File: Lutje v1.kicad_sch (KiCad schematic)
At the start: 9 parts, among them J1 U.FL-R-SMT_10_, U1 ESP32-S3FH4R2, U2 SX1281IMLTRT, U3 AMS1117-3.3, U4 DRV8212DRLR, U5 DRV8212DRLR, U6 DRV8212DRLR

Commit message: initial schematic work
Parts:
- removed FL1: 2450FM07D0034T, footprints:FIL_2450FM07D0034T, symbol 2450FM07D0034T:2450FM07D0034T
- removed J1: U.FL-R-SMT_10_, footprints:HIROSE_U.FL-R-SMT_10_, symbol U.FL-R-SMT_10_:U.FL-R-SMT_10_
- removed U1: ESP32-S3FH4R2, footprints:QFN40P700X700X90-57N, symbol ESP32-S3FH4R2:ESP32-S3FH4R2
- removed U2: SX1281IMLTRT, footprints:XCVR_SX1281IMLTRT, symbol SX1281IMLTRT:SX1281IMLTRT
- removed U3: AMS1117-3.3, footprints:SOT229P700X180-4N, symbol AMS1117-3.3:AMS1117-3.3
- removed U4, U5, U6: DRV8212DRLR, footprints:drv8212drlr, symbol drv8212drlr:DRV8212DRLR
- removed XTAL1: NX2016SA-52MHZ-EXS00A-CS07103, footprints:OSCCC200X160X50N, symbol NX2016SA-52MHZ-EXS00A-CS07103:NX2016SA-52MHZ-EXS00A-CS07103
- added C1, C4: 10n, symbol Device:C
- added C10, C11, C6, C7, C8, C9: C, symbol Device:C
- added C2, C3: 100n, symbol Device:C
- added C5: 470n, symbol Device:C
- added J1, J3, J4, J5: Conn_01x02, symbol Connector_Generic:Conn_01x02
- added J2: Conn_Coaxial, Connector_Coaxial:U.FL_Hirose_U.FL-R-SMT-1_Vertical, symbol Connector:Conn_Coaxial
- added U1: SX1280, Package_DFN_QFN:QFN-24-1EP_4x4mm_P0.5mm_EP2.7x2.7mm, symbol .local:SX1280
- added U11, U12, U7: DRV8212DRL, Package_TO_SOT_SMD:SOT-563, symbol .local:DRV8212DRL
- added U2: 2450FM07D0034, symbol .local:2450FM07D0034
- added U3: ESP32-S3S3FN8, Package_DFN_QFN:QFN-56-1EP_7x7mm_P0.4mm_EP5.6x5.6mm, symbol PCM_Espressif:ESP32-S3
- added U8: AMS1117-3.3, Package_TO_SOT_SMD:SOT-223-3_TabPin2, symbol Regulator_Linear:AMS1117-3.3
- added Y1: XC21M4-52.000-F10NNHPL, symbol Device:Crystal_GND24
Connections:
- net GND: now also C1.2, C10.2, C11.2, C2.2, C3.2, C4.2, C5.2, C6.2, C7.2, C8.2, C9.2, J5.1 (Pin_1), U1.13 (GND), U1.20 (GND), U1.21 (GND), U1.23 (GND), U1.24 (GND), U1.25 (GND), U1.5 (GND), U11.3 (GND), U12.3 (GND), U2.2 (GND), U2.4 (GND), U7.3 (GND), U8.1 (GND), Y1.2 (G), Y1.4 (G)
- net VDD3P3: now also U3.2 (VDD3P3), U3.3 (VDD3P3)
- new net: U3.55 (VDDA), U3.56 (VDDA)
- new net +3V3: C2.1, C3.1, C7.1, U1.11 (VBAT_IO), U1.15 (VBAT), U8.2 (VO)
- new net VDC: C10.1, C11.1, C6.1, C8.1, C9.1, J5.2 (Pin_2), U11.5 (VM), U12.5 (VM), U7.5 (VM), U8.3 (VI)
- new net m0_in1: U7.1 (IN1)
- new net m0_in2: U7.2 (IN2)
- new net m0_out1: J1.1 (Pin_1), U7.6 (OUT1)
- new net m0_out2: J1.2 (Pin_2), U7.4 (OUT2)
- new net m1_in1: U11.1 (IN1)
- new net m1_in2: U11.2 (IN2)
- new net m1_out1: J3.1 (Pin_1), U11.6 (OUT1)
- new net m1_out2: J3.2 (Pin_2), U11.4 (OUT2)
- new net m2_in1: U12.1 (IN1)
- new net m2_in2: U12.2 (IN2)
- new net m2_out1: J4.1 (Pin_1), U12.6 (OUT1)
- new net m2_out2: J4.2 (Pin_2), U12.4 (OUT2)
- new net rfio: U1.22 (RFIO), U2.1 (IN)
- new net sx1280_dcc_fb/vdd_in: C4.1, C5.1, U1.12 (DCC_FB), U1.2 (VDD_IN)
- new net sx1280_xta: U1.4 (XTA), Y1.1
- new net sx1280_xtb: U1.6 (XTB), Y1.3
- new net vr_pa: C1.1, U1.1 (VR_PA)
- no-connect marks 0 -> 1
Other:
- note added: "als we maar 2 brushed kanalen willen kunenn we een c3 gebruiken"
- note added: "datasheet beveeld 22uF tantalum aan bij de output. tantalum is irritant en heeft een varierende prijs het is het overwegen waardt om die te vervangen met een keramische mogelijk met een series resisotr om de hogere ESR te simuleren als dat nodig is voor stability. ook DC-bias effecten controleren maar ik vermoed dat dat niet een heel erg groot probleem is bij 3.3V"
- note added: "er moet hier een rf-switch tussen zodat er ook een pcb antenne bij kan"
- note added: "is een bulk capacitor nodig? en hoe groot moet hij dan zijn?"
- note added: "overweeg reverse polarity protection. en maybe een zekering"

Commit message: begin esp inrichting gemaakt
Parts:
- removed J4: Conn_01x02, symbol Connector_Generic:Conn_01x02
- removed U12: DRV8212DRL, Package_TO_SOT_SMD:SOT-563, symbol .local:DRV8212DRL
- added AE1: Antenna, symbol Device:Antenna
- added C12, C17: 1uF, symbol Device:C
- added C13: 10uF, symbol Device:C
- added C14, C15, C18, C25: 100n, symbol Device:C
- added C16: 10n, symbol Device:C
- added C19, C20: TBD, symbol Device:C
- added C21, C22, C23, C24: C, symbol Device:C
- added D1: PWR, symbol Device:LED
- added D2: LED, symbol Device:LED
- added L1: 2.0 nH 500 mA, symbol Device:L
- added L2: TBD, symbol Device:L
- added L3, L4: L, symbol Device:L
- added Q1: AON7403, AON7403:TRANS_AON7403, symbol AON7403:AON7403
- added R1: 10R, symbol Device:R
- added R2: 33R, symbol Device:R
- added R3: 33K, symbol Device:R
- added R4, R5, R6: 10K, symbol Device:R
- added R7, R8: 1K, symbol Device:R
- added SW1: SW_Push, symbol Switch:SW_Push
- added Y2: XXDBBCNANF-40.000000MHZ, symbol Device:Crystal_GND24
- C10, C11: value C -> 100n
- C6: value C -> 10uF
- C7: value C -> 22uF
- J2: footprint Connector_Coaxial:U.FL_Hirose_U.FL-R-SMT-1_Vertical -> (none)
- Y1: lcsc C3034316 -> (none)
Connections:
- net +3V3: now also C11.1, U3.20 (VDD3P3_RTC), U3.46 (VDD3P3_CPU), U3.55 (VDDA), U3.56 (VDDA), C12.1, C13.1, C14.2, C15.2, C16.2, C17.2, D1.2 (A), D2.2 (A), L1.1, R5.2, R6.1
- net GND: now also C12.2, C13.2, C14.1, C15.1, C16.1, C17.1, C18.1, C19.2, C20.2, C21.2, C22.2, C23.2, C24.2, C25.2, R1.2, R4.2, R7.1, SW1.2, Y2.2 (G), Y2.4 (G)
- net VDC: now also Q1.1, Q1.2, Q1.3, R3.1; no longer C10.1, C11.1, J5.2 (Pin_2)
- net VDD3P3: now also C10.1, L1.2
- net at U3.1 (LNA_IN/RF): now also C24.1, L4.2
- net SX1280_RESET: now reaches U3.13 (GPIO8/ADC1_CH7)
- net SX1280_RESET: now also U1.3 (~{RESET})
- net SX1280_DIO1: now reaches U3.14 (GPIO9/ADC1_CH8)
- net SX1280_DIO1: now also U1.8 (DIO1)
- net SS_CTS: now reaches U3.15 (GPIO10/ADC1_CH9)
- net SS_CTS: now also U1.19 (~{SS_CTS})
- net SX1280_MOSI: now reaches U3.16 (GPIO11/ADC2_CH0)
- net SX1280_MOSI: now also U1.17 (MOSI_RX)
- net at U3.17 (GPIO12/ADC2_CH1): now also R2.1
- net SX1280_MISO: now reaches U3.18 (GPIO13/ADC2_CH2)
- net SX1280_MISO: now also U1.16 (MISO_TX)
- net SX1280_BUSY: now reaches U3.19 (GPIO14/ADC2_CH3)
- net SX1280_BUSY: now also U1.7 (BUSY)
- net at U3.29 (VDD_SPI): now also C18.2
- net at U3.4 (CHIP_PU/RESET): now also C25.1, R5.1
- net BOOT: now reaches U3.5 (GPIO0/BOOT)
- net BOOT: now also R6.2, SW1.1
- net at U3.53 (XTAL_N): now also C19.1, Y2.3
- net at U3.54 (XTAL_P): now also L2.2
- net VSENS: now reaches U3.6 (GPIO1/ADC1_CH0)
- net VSENS: now also R3.2, R4.1
- net at U3.7 (GPIO2/ADC1_CH1): now also R8.2
- net SCK: now reaches U1.18 (SCK_~{RTS})
- net SCK: now also R2.2
- net rfio renamed SX1280_RFIO
- net sx1280_dcc_fb/vdd_in renamed SX1280_DCC_FB/VDD_IN
- net sx1280_xta renamed SX1280_XTA
- net sx1280_xtb renamed SX1280_XTB
- net vr_pa renamed SX1280_VR_PA
- new net: C22.1, C23.1, L3.2, L4.1
- new net: C20.1, L2.1, Y2.1
- new net: AE1.1 (A), C21.1, L3.1
- new net: D1.1 (K), R7.2
- new net: Q1.4, R1.1
- new net: J5.2 (Pin_2), Q1.5_8
- new net: D2.1 (K), R8.1
- no-connect marks 1 -> 3
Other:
- note removed: "als we maar 2 brushed kanalen willen kunenn we een c3 gebruiken"
- note removed: "is een bulk capacitor nodig? en hoe groot moet hij dan zijn?"
- note removed: "overweeg reverse polarity protection. en maybe een zekering"
- moved on the sheet: C1, C2, C3, C4, C5, C8, C9, J1, J2, J3, U1, U11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

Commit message: begin esp inrichting gemaakt
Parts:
- U3: value ESP32-S3S3FN8 -> ESP32-S3FN8
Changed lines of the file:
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@@
 			)
 		)
-		(property "Value" "ESP32-S3S3FN8"
+		(property "Value" "ESP32-S3FN8"
 			(at 239.6333 198.12 0)
 			(show_name no)

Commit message: aanpassing aan schematic
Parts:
- removed R2: 33R, symbol Device:R
- removed R6: 10K, symbol Device:R
- Y2: value XXDBBCNANF-40.000000MHZ -> Q22FA12800332; footprint (none) -> Crystal:Crystal_SMD_2016-4Pin_2.0x1.6mm; lcsc (none) -> C255899
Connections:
- net GND: now also U3.57 (GND); no longer C10.2, C11.2, C12.2, C13.2, C18.1
- net SCK: now also U3.17 (GPIO12/ADC2_CH1)
- net lna_matching: now reaches C22.1, C23.1, L3.2, L4.1
- net esp32_xtal_p: now reaches C20.1, L2.1, Y2.1
- net esp32_xtal_n: now reaches C19.1, U3.53 (XTAL_N), Y2.3
- net lna_ant: now reaches AE1.1 (A), C21.1, L3.1
- net chip_pu: now reaches C25.1, R5.1, U3.4 (CHIP_PU/RESET)
- net status_LED_n0: now reaches D2.1 (K), R8.1
- net vdd_spi: now reaches C18.2, U3.29 (VDD_SPI)
- net lna_in: now reaches C24.1, L4.2, U3.1 (LNA_IN/RF)
- net esp32_xtal_p_filtered: now reaches L2.2, U3.54 (XTAL_P)
- net STATUS_LED: now reaches R8.2, U3.7 (GPIO2/ADC1_CH1)
- new net: C10.2, C11.2, C12.2, C13.2, C18.1
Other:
- moved on the sheet: C19, C20, D2, L2, R3, R4, R8, SW1, Y2

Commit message: changed to esp32, added zener/tvs and servo channels
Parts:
- removed AE1: Antenna, symbol Device:Antenna
- removed C24: C, symbol Device:C
- removed C25: 100n, symbol Device:C
- removed L2: TBD, symbol Device:L
- removed L3, L4: L, symbol Device:L
- removed U3: ESP32-S3FN8, Package_DFN_QFN:QFN-56-1EP_7x7mm_P0.4mm_EP5.6x5.6mm, symbol PCM_Espressif:ESP32-S3
- added AE1: Antenna_Chip, symbol Device:Antenna_Chip
- added D3, D4: D_Zener, symbol Device:D_Zener
- added D5: D_TVS, symbol Device:D_TVS
- added J4: Conn_01x02, symbol Connector_Generic:Conn_01x02
- added J6, J8: Conn_01x03, symbol Connector_Generic:Conn_01x03
- added R2: R, symbol Device:R
- added R6: 1k, symbol Device:R
- added U3: ESP32-U4WDH, .local:esp32_2layer_thermalvias, symbol PCM_Espressif:ESP32
- C10, C11, C14, C15: value 100n -> TBD; footprint (none) -> Capacitor_SMD:C_0402_1005Metric
- C12, C17: value 1uF -> 10u; footprint (none) -> Capacitor_SMD:C_0402_1005Metric
- C13: value 10uF -> 10u; footprint (none) -> Capacitor_SMD:C_0402_1005Metric
- C16: value 10n -> 10u; footprint (none) -> Capacitor_SMD:C_0402_1005Metric
- C18: value 100n -> 10u; footprint (none) -> Capacitor_SMD:C_0402_1005Metric
- C19, C20: value TBD -> 10u; footprint (none) -> Capacitor_SMD:C_0402_1005Metric
- C21, C23: value C -> 10u; footprint (none) -> Capacitor_SMD:C_0402_1005Metric
- C22: value C -> 10n; footprint (none) -> Capacitor_SMD:C_0402_1005Metric
- L1: value 2.0 nH 500 mA -> TBD
- R5: value 10K -> 1k
- R8: value 1K -> 10k; footprint (none) -> Resistor_SMD:R_0402_1005Metric
- Y2: value Q22FA12800332 -> 40Mhz; footprint Crystal:Crystal_SMD_2016-4Pin_2.0x1.6mm -> (none); lcsc C255899 -> C655053; private KLC_S4.1 -> (none)
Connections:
- net lna_ant is gone; now on net +3V3: C21.1
- net vdd_spi is gone; now on net GND: C18.2
- net +3V3: now also C16.1, C17.1, C18.1, C19.1, C20.1, R8.1, U3.1 (VDDA), U3.19 (VDD3P3_RTC), U3.3 (VDD3P3), U3.37 (VDD3P3_CPU), U3.4 (VDD3P3), U3.43 (VDDA), U3.46 (VDDA); no longer C11.1, C12.1, C14.2, C15.2, C16.2, C17.2, D2.2 (A), L1.1, R5.2
- net GND: now also C10.2, C11.2, C12.2, C13.2, C14.2, C15.2, C16.2, C17.2, D2.1 (K), AE1.1 (FEED), D3.2 (A), D4.2 (A), D5.1 (A1), J6.3 (Pin_3), J8.3 (Pin_3), U3.49 (GND); no longer C14.1, C15.1, C16.1, C17.1
- net VDC: now also J6.1 (Pin_1), J8.1 (Pin_1)
- net m0_in1: no longer U7.1 (IN1)
- net m0_in2: no longer U7.2 (IN2)
- net at J5.2 (Pin_2), Q1.5_8: now also D5.2 (A2)
- net BOOT: no longer names the net of SW1.1
- net BOOT: now also U3.23 (GPIO0/BOOT/ADC2_CH1)
- net STATUS_LED renamed esp32_chip_pu
- net esp32_chip_pu: now also C23.1, U3.9 (CHIP_PU)
- net VDD3P3 renamed ant_esp
- net ant_esp: now also L1.1, AE1.2 (PCB_Trace); no longer L1.2
- net chip_pu renamed esp_ch3
- net esp_ch3: now also D4.1 (K)
- net esp32_xtal_n renamed xtaln
- net xtaln: now also C14.1, U3.44 (XTAL_N); no longer C19.1
- net esp32_xtal_p renamed xtalp
- net xtalp: now also C15.1, U3.45 (XTAL_P); no longer C20.1
- net lna_matching: no longer names the net of C22.1
- net lna_matching: now also U3.47 (CAP2), U3.48 (CAP1); no longer C23.1
- net m0_out1 renamed m2_out1
- net m0_out2 renamed m2_out2
- removed net status_LED_n0: D2.1 (K), R8.1
- new net: C12.1, U3.26 (VDD_SDIO)
- new net ant_esp_in: C11.1, L1.2, U3.2 (LNA_IN)
- new net ch3: J6.2 (Pin_2), R5.2
- new net ch4: J8.2 (Pin_2), R6.2
- new net esp_ch4: D3.1 (K), R6.1
- new net m2_in1: U7.1 (IN1)
- new net m2_in2: U7.2 (IN2)
- new net status_led: R2.1
- new net status_led_n0: D2.2 (A), R2.2
- new net u0rx: J4.2 (Pin_2), U3.40 (U0RXD/GPIO3)
- new net u0tx: J4.1 (Pin_1), U3.41 (U0TXD/GPIO1)
- no-connect marks 3 -> 9
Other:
- note added: "1612 crystal kan veranderd worden"
- note added: "<- deze reeks pins (behalve 28/20) zijn verbonden aan de flash. Niet gebruiken"
- note added: "<- strapping pin. (interne) pulldown"
- note added: "check of de default status van de pins niet een motor laten draaien"
- note added: "strapping pin (u0txd). (interne) pullup ->"
- note added: "strapping pin vdd_sdio. (interne) pulldown ->"
- moved on the sheet: C1, C2, C3, C4, C5, C8, C9, J1, J2, J3, R3, R4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

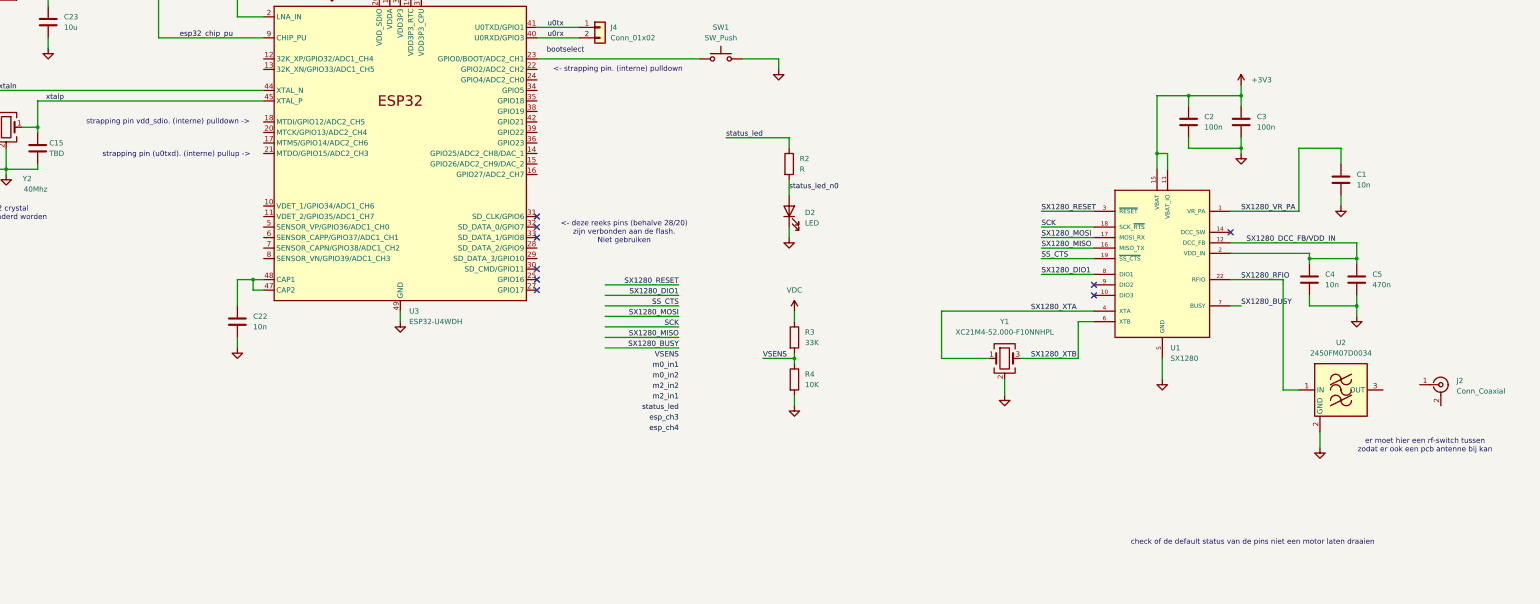
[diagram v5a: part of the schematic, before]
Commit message: antenne jumpers. wat footprint assignments
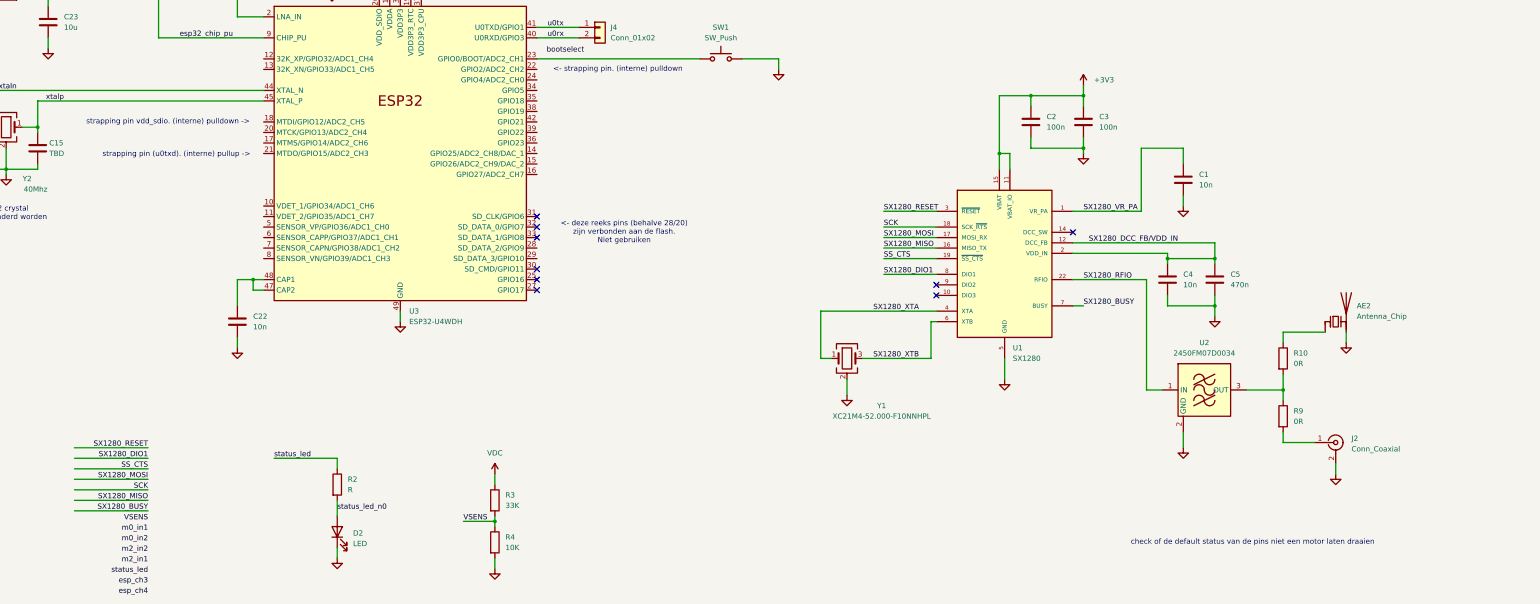
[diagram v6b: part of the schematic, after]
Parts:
- removed U3: ESP32-U4WDH, .local:esp32_2layer_thermalvias, symbol PCM_Espressif:ESP32
- added AE2: Antenna_Chip, symbol Device:Antenna_Chip
- added R10, R9: 0R, Resistor_SMD:R_0402_1005Metric, symbol Device:R
- added U3: ESP32-U4WDH, symbol .local:ESP32-U4WDH
- C2, C3, C4, C5, R7: footprint (none) -> Capacitor_SMD:C_0402_1005Metric
- D1, D2: footprint (none) -> LED_SMD:LED_0603_1608Metric
- J1: footprint (none) -> Footprint 0 0 Center Center 0 0
- J6, J8: footprint (none) -> Connector_PinHeader_2.54mm:PinHeader_1x03_P2.54mm_Vertical
- L1: footprint (none) -> Inductor_SMD:L_0402_1005Metric
- R1, R2, R3, R4, R5, R6: footprint (none) -> Resistor_SMD:R_0402_1005Metric
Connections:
- net +3V3: now also U3.1 (VDDA), U3.19 (VDD3P3_RTC), U3.3 (VDD3P3), U3.37 (VDD3P3_CPU), U3.4 (VDD3P3), U3.43 (VDDA), U3.46 (VDDA)
- net GND: now also J2.2 (Ext), AE2.2 (PCB_Trace), U3.49 (GND)
- net ant_esp_in: now also U3.2 (LNA_IN)
- net esp32_chip_pu: now also U3.9 (CHIP_PU)
- net u0rx: now also U3.40 (U0RXD/GPIO3)
- net u0tx: now also U3.41 (U0TXD/GPIO1)
- net xtaln: now also U3.44 (XTAL_N)
- net xtalp: now also U3.45 (XTAL_P)
- net at SW1.1: now also U3.23 (GPIO0/BOOT/ADC2_CH1)
- net at C12.1: now also U3.26 (VDD_SDIO)
- net at C22.1: now also U3.47 (CAP2), U3.48 (CAP1)
- net at U2.3 (OUT): now also R10.2, R9.1
- net at J2.1 (In): now also R9.2
- new net: AE2.1 (FEED), R10.1
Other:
- note removed: "er moet hier een rf-switch tussen zodat er ook een pcb antenne bij kan"
- moved on the sheet: C1, C2, C3, C4, C5, D2, J2, R2, R3, R4, U1, U2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

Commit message: more footprint work
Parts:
- C1: footprint (none) -> Capacitor_SMD:C_0402_1005Metric
- J1: footprint Footprint 0 0 Center Center 0 0 -> Connector_PinHeader_2.54mm:PinHeader_1x02_P2.54mm_Vertical
- J2: footprint (none) -> Connector_Coaxial:U.FL_Hirose_U.FL-R-SMT-1_Vertical
- J3, J4, J5: footprint (none) -> Connector_PinHeader_2.54mm:PinHeader_1x02_P2.54mm_Vertical
- U2: footprint (none) -> .local:2450FM07D0034001T
- Y1: footprint (none) -> Crystal:Crystal_SMD_2016-4Pin_2.0x1.6mm; lcsc (none) -> C3034316
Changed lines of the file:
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@@
 			)
 		)
-		(property "Footprint" ""
+		(property "Footprint" "Connector_PinHeader_2.54mm:PinHeader_1x02_P2.54mm_Vertical"
 			(at 387.35 50.8 0)
 			(hide yes)
@@
 			)
 		)
-		(property "Footprint" ""
+		(property "Footprint" ".local:2450FM07D0034001T"
 			(at 323.85 233.68 0)
 			(hide yes)
@@
 			)
 		)
-		(property "Footprint" ""
+		(property "Footprint" "Connector_PinHeader_2.54mm:PinHeader_1x02_P2.54mm_Vertical"
 			(at 177.8 134.62 0)
 			(hide yes)
@@
 			)
 		)
-		(property "Footprint" ""
+		(property "Footprint" "Connector_PinHeader_2.54mm:PinHeader_1x02_P2.54mm_Vertical"
 			(at 44.45 66.04 0)
 			(hide yes)
@@
 			)
 		)
-		(property "Footprint" ""
+		(property "Footprint" "Connector_Coaxial:U.FL_Hirose_U.FL-R-SMT-1_Vertical"
 			(at 355.6 234.95 0)
 			(hide yes)
@@
 			)
 		)
-		(property "Footprint" ""
+		(property "Footprint" "Capacitor_SMD:C_0402_1005Metric"
 			(at 319.7352 175.26 0)
 			(hide yes)
@@
 			)
 		)
-		(property "Footprint" "Footprint  0 0 Center Center 0 0"
+		(property "Footprint" "Connector_PinHeader_2.54mm:PinHeader_1x02_P2.54mm_Vertical"
 			(at 387.35 107.95 0)
 			(hide yes)
@@
 			)
 		)
-		(property "Footprint" ""
+		(property "Footprint" "Crystal:Crystal_SMD_2016-4Pin_2.0x1.6mm"
 			(at 237.49 214.63 0)
 			(hide yes)
@@
 			(do_not_autoplace no)
 			(effects
+				(font
+					(size 1.27 1.27)
+				)
+			)
+		)
+		(property "lcsc" "C3034316"
+			(at 237.49 214.63 0)
+			(hide yes)
+			(show_name no)
+			(do_not_autoplace no)
+			(effects

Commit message: 1612 crystal
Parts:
- Y2: footprint (none) -> .local:SMD1612_crystal
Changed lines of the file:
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@@
 			)
 		)
-		(property "Footprint" ""
+		(property "Footprint" ".local:SMD1612_crystal"
 			(at 34.29 158.75 0)
 			(hide yes)
